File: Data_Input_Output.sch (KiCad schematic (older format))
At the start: 38 parts, among them K1 G5LE_1A4_DC3, K2 G5LE_1A4_DC3, P10 CONN_01X02, P11 CONN_01X02, P12 CONN_01X02, P3 CONN_01X04, P4 CONN_01X04, P5 CONN_01X04, P6 CONN_01X04, P7 CONN_01X02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

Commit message: completed first revision of the board.
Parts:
- P10, P11, P12, P7, P8, P9: footprint Connectors_JST:JST_PH_B2B-PH-K_02x2.00mm_Straight -> SPEX_Parts:ultraFitCONN_2
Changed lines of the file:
@@
 $EndDescr
 $Comp
-L GND #PWR062
+L GND #PWR063
 U 1 1 56EB177F
 P 5450 2550
-F 0 "#PWR062" H 5450 2300 50  0001 C CNN
+F 0 "#PWR063" H 5450 2300 50  0001 C CNN
 F 1 "GND" H 5450 2400 50  0000 C CNN
 F 2 "" H 5450 2550 60  0000 C CNN
@@
 Data_GND
 $Comp
-L +3.3V #PWR063
+L +3.3V #PWR064
 U 1 1 56EB1E10
 P 2500 950
-F 0 "#PWR063" H 2500 800 50  0001 C CNN
+F 0 "#PWR064" H 2500 800 50  0001 C CNN
 F 1 "+3.3V" H 2500 1090 50  0000 C CNN
 F 2 "" H 2500 950 60  0000 C CNN
@@
 $EndComp
 $Comp
-L GND #PWR064
+L GND #PWR065
 U 1 1 56EB1E33
 P 2500 1200
-F 0 "#PWR064" H 2500 950 50  0001 C CNN
+F 0 "#PWR065" H 2500 950 50  0001 C CNN
 F 1 "GND" H 2500 1050 50  0000 C CNN
 F 2 "" H 2500 1200 60  0000 C CNN
@@
 $EndComp
 $Comp
-L +3.3V #PWR065
+L +3.3V #PWR066
 U 1 1 56EB2146
 P 2550 2650
-F 0 "#PWR065" H 2550 2500 50  0001 C CNN
+F 0 "#PWR066" H 2550 2500 50  0001 C CNN
 F 1 "+3.3V" H 2550 2790 50  0000 C CNN
 F 2 "" H 2550 2650 60  0000 C CNN
@@
 $EndComp
 $Comp
-L GND #PWR066
+L GND #PWR067
 U 1 1 56EB216C
 P 2550 3950
-F 0 "#PWR066" H 2550 3700 50  0001 C CNN
+F 0 "#PWR067" H 2550 3700 50  0001 C CNN
 F 1 "GND" H 2550 3800 50  0000 C CNN
 F 2 "" H 2550 3950 60  0000 C CNN
@@
 $EndComp
 $Comp
-L GND #PWR067
+L GND #PWR068
 U 1 1 56EBFD84
 P 1900 5500
-F 0 "#PWR067" H 1900 5250 50  0001 C CNN
+F 0 "#PWR068" H 1900 5250 50  0001 C CNN
 F 1 "GND" H 1900 5350 50  0000 C CNN
 F 2 "" H 1900 5500 60  0000 C CNN
@@
 $EndComp
 $Comp
-L +3.3V #PWR068
+L +3.3V #PWR069
 U 1 1 56EBFDB9
 P 1900 4100
-F 0 "#PWR068" H 1900 3950 50  0001 C CNN
+F 0 "#PWR069" H 1900 3950 50  0001 C CNN
 F 1 "+3.3V" H 1900 4240 50  0000 C CNN
 F 2 "" H 1900 4100 60  0000 C CNN
@@
 SD_MISO
 $Comp
-L +3.3V #PWR069
+L +3.3V #PWR070
 U 1 1 56F427AD
 P 5400 1000
-F 0 "#PWR069" H 5400 850 50  0001 C CNN
+F 0 "#PWR070" H 5400 850 50  0001 C CNN
 F 1 "+3.3V" H 5400 1140 50  0000 C CNN
 F 2 "" H 5400 1000 60  0000 C CNN
@@
 $EndComp
 $Comp
-L +3.3V #PWR070
+L +3.3V #PWR071
 U 1 1 56F4344F
 P 6200 1600
-F 0 "#PWR070" H 6200 1450 50  0001 C CNN
+F 0 "#PWR071" H 6200 1450 50  0001 C CNN
 F 1 "+3.3V" H 6200 1740 50  0000 C CNN
 F 2 "" H 6200 1600 60  0000 C CNN
@@
 $EndComp
 $Comp
-L GND #PWR071
+L GND #PWR072
 U 1 1 56F43490
 P 6200 2400
-F 0 "#PWR071" H 6200 2150 50  0001 C CNN
+F 0 "#PWR072" H 6200 2150 50  0001 C CNN
 F 1 "GND" H 6200 2250 50  0000 C CNN
 F 2 "" H 6200 2400 60  0000 C CNN
@@
 SD_PWRCTRL
 $Comp
-L GND #PWR072
+L GND #PWR073
 U 1 1 56F6549F
 P 5950 3700
-F 0 "#PWR072" H 5950 3450 50  0001 C CNN
+F 0 "#PWR073" H 5950 3450 50  0001 C CNN
 F 1 "GND" H 5950 3550 50  0000 C CNN
 F 2 "" H 5950 3700 60  0000 C CNN
@@
 $EndComp
 $Comp
-L GND #PWR073
+L GND #PWR074
 U 1 1 56F66682
 P 5950 4650
-F 0 "#PWR073" H 5950 4400 50  0001 C CNN
+F 0 "#PWR074" H 5950 4400 50  0001 C CNN
 F 1 "GND" H 5950 4500 50  0000 C CNN
 F 2 "" H 5950 4650 60  0000 C CNN
@@
 $EndComp
 $Comp
-L GND #PWR074
+L GND #PWR075
 U 1 1 56F669B0
 P 5950 5600
-F 0 "#PWR074" H 5950 5350 50  0001 C CNN
+F 0 "#PWR075" H 5950 5350 50  0001 C CNN
 F 1 "GND" H 5950 5450 50  0000 C CNN
 F 2 "" H 5950 5600 60  0000 C CNN
@@
 Relay_2
 $Comp
-L +3.3V #PWR075
+L +3.3V #PWR076
 U 1 1 56F72165
 P 2850 6400
-F 0 "#PWR075" H 2850 6250 50  0001 C CNN
+F 0 "#PWR076" H 2850 6250 50  0001 C CNN
 F 1 "+3.3V" H 2850 6540 50  0000 C CNN
 F 2 "" H 2850 6400 60  0000 C CNN
@@
 $EndComp
 $Comp
-L +3.3V #PWR076
+L +3.3V #PWR077
 U 1 1 56F721B8
 P 5950 6400
-F 0 "#PWR076" H 5950 6250 50  0001 C CNN
+F 0 "#PWR077" H 5950 6250 50  0001 C CNN
 F 1 "+3.3V" H 5950 6540 50  0000 C CNN
 F 2 "" H 5950 6400 60  0000 C CNN
@@
 $EndComp
 $Comp
-L GND #PWR077
+L GND #PWR078
 U 1 1 56F72343
 P 1850 7600
-F 0 "#PWR077" H 1850 7350 50  0001 C CNN
+F 0 "#PWR078" H 1850 7350 50  0001 C CNN
 F 1 "GND" H 1850 7450 50  0000 C CNN
 F 2 "" H 1850 7600 60  0000 C CNN
@@
 $EndComp
 $Comp
-L GND #PWR078
+L GND #PWR079
 U 1 1 56F72396
 P 4950 7600
-F 0 "#PWR078" H 4950 7350 50  0001 C CNN
+F 0 "#PWR079" H 4950 7350 50  0001 C CNN
 F 1 "GND" H 4950 7450 50  0000 C CNN
 F 2 "" H 4950 7600 60  0000 C CNN
@@
 F 0 "P7" H 10350 3600 50  0000 C CNN
 F 1 "CONN_01X02" V 10450 3450 50  0000 C CNN
-F 2 "Connectors_JST:JST_PH_B2B-PH-K_02x2.00mm_Straight" H 10350 3450 50  0001 C CNN
+F 2 "SPEX_Parts:ultraFitCONN_2" H 10350 3450 50  0001 C CNN
 F 3 "" H 10350 3450 50  0000 C CNN
 	1    10350 3450
@@
 F 0 "P8" H 10350 4100 50  0000 C CNN
 F 1 "CONN_01X02" V 10450 3950 50  0000 C CNN
-F 2 "Connectors_JST:JST_PH_B2B-PH-K_02x2.00mm_Straight" H 10350 3950 50  0001 C CNN
+F 2 "SPEX_Parts:ultraFitCONN_2" H 10350 3950 50  0001 C CNN
 F 3 "" H 10350 3950 50  0000 C CNN
 	1    10350 3950
@@
 F 0 "P9" H 10350 4600 50  0000 C CNN
 F 1 "CONN_01X02" V 10450 4450 50  0000 C CNN
-F 2 "Connectors_JST:JST_PH_B2B-PH-K_02x2.00mm_Straight" H 10350 4450 50  0001 C CNN
+F 2 "SPEX_Parts:ultraFitCONN_2" H 10350 4450 50  0001 C CNN
 F 3 "" H 10350 4450 50  0000 C CNN
 	1    10350 4450
@@
 F 0 "P10" H 10350 5100 50  0000 C CNN
 F 1 "CONN_01X02" V 10450 4950 50  0000 C CNN
-F 2 "Connectors_JST:JST_PH_B2B-PH-K_02x2.00mm_Straight" H 10350 4950 50  0001 C CNN
+F 2 "SPEX_Parts:ultraFitCONN_2" H 10350 4950 50  0001 C CNN
 F 3 "" H 10350 4950 50  0000 C CNN
 	1    10350 4950
@@
 F 0 "P11" H 10350 5600 50  0000 C CNN
 F 1 "CONN_01X02" V 10450 5450 50  0000 C CNN
-F 2 "Connectors_JST:JST_PH_B2B-PH-K_02x2.00mm_Straight" H 10350 5450 50  0001 C CNN
+F 2 "SPEX_Parts:ultraFitCONN_2" H 10350 5450 50  0001 C CNN
 F 3 "" H 10350 5450 50  0000 C CNN
 	1    10350 5450
@@
 F 0 "P12" H 10350 6150 50  0000 C CNN
 F 1 "CONN_01X02" V 10450 6000 50  0000 C CNN
-F 2 "Connectors_JST:JST_PH_B2B-PH-K_02x2.00mm_Straight" H 10350 6000 50  0001 C CNN
+F 2 "SPEX_Parts:ultraFitCONN_2" H 10350 6000 50  0001 C CNN
 F 3 "" H 10350 6000 50  0000 C CNN
 	1    10350 6000
@@
 	10050 6050 10150 6050
 $Comp
-L GND #PWR079
+L GND #PWR080
 U 1 1 57038625
 P 9450 2600
-F 0 "#PWR079" H 9450 2350 50  0001 C CNN
+F 0 "#PWR080" H 9450 2350 50  0001 C CNN
 F 1 "GND" H 9450 2450 50  0000 C CNN
 F 2 "" H 9450 2600 60  0000 C CNN
@@
 $EndComp
 $Comp
-L GND #PWR080
+L GND #PWR081
 U 1 1 5703869C
 P 9450 1700
-F 0 "#PWR080" H 9450 1450 50  0001 C CNN
+F 0 "#PWR081" H 9450 1450 50  0001 C CNN
 F 1 "GND" H 9450 1550 50  0000 C CNN
 F 2 "" H 9450 1700 60  0000 C CNN
@@
 	9450 2500 9450 2600
 $Comp
-L +3.3V #PWR081
+L +3.3V #PWR082
 U 1 1 57038AFB
 P 9450 1200
-F 0 "#PWR081" H 9450 1050 50  0001 C CNN
+F 0 "#PWR082" H 9450 1050 50  0001 C CNN
 F 1 "+3.3V" H 9450 1340 50  0000 C CNN
 F 2 "" H 9450 1200 60  0000 C CNN
@@
 $EndComp
 $Comp
-L +3.3V #PWR082
+L +3.3V #PWR083
 U 1 1 57038B72
 P 9450 2100
-F 0 "#PWR082" H 9450 1950 50  0001 C CNN
+F 0 "#PWR083" H 9450 1950 50  0001 C CNN
 F 1 "+3.3V" H 9450 2240 50  0000 C CNN
 F 2 "" H 9450 2100 60  0000 C CNN
@@
 $EndComp
 $Comp
-L +3.3V #PWR083
+L +3.3V #PWR084
 U 1 1 57039D7A
 P 8300 1200
-F 0 "#PWR083" H 8300 1050 50  0001 C CNN
+F 0 "#PWR084" H 8300 1050 50  0001 C CNN
 F 1 "+3.3V" H 8300 1340 50  0000 C CNN
 F 2 "" H 8300 1200 60  0000 C CNN
@@
 $EndComp
 $Comp
-L GND #PWR084
+L GND #PWR085
 U 1 1 57039E1D
 P 8300 1700
-F 0 "#PWR084" H 8300 1450 50  0001 C CNN
+F 0 "#PWR085" H 8300 1450 50  0001 C CNN
 F 1 "GND" H 8300 1550 50  0000 C CNN
 F 2 "" H 8300 1700 60  0000 C CNN
@@
 $EndComp
 $Comp
-L +3.3V #PWR085
+L +3.3V #PWR086
 U 1 1 57033FCB
 P 8300 2100
-F 0 "#PWR085" H 8300 1950 50  0001 C CNN
+F 0 "#PWR086" H 8300 1950 50  0001 C CNN
 F 1 "+3.3V" H 8300 2240 50  0000 C CNN
 F 2 "" H 8300 2100 60  0000 C CNN
@@
 $EndComp
 $Comp
-L GND #PWR086
+L GND #PWR087
 U 1 1 57033FD1
 P 8300 2600
-F 0 "#PWR086" H 8300 2350 50  0001 C CNN
+F 0 "#PWR087" H 8300 2350 50  0001 C CNN
 F 1 "GND" H 8300 2450 50  0000 C CNN
 F 2 "" H 8300 2600 60  0000 C CNN
@@
 UART_RX_out
 $Comp
-L +3.3V #PWR087
+L +3.3V #PWR088
 U 1 1 570406FF
 P 10000 3300
-F 0 "#PWR087" H 10000 3150 50  0001 C CNN
+F 0 "#PWR088" H 10000 3150 50  0001 C CNN
 F 1 "+3.3V" H 10000 3440 50  0000 C CNN
 F 2 "" H 10000 3300 60  0000 C CNN
@@
 	10000 3300 10000 3500
 $Comp
-L +5V #PWR088
+L +5V #PWR089
 U 1 1 57040BC0
 P 10000 3800
-F 0 "#PWR088" H 10000 3650 50  0001 C CNN
+F 0 "#PWR089" H 10000 3650 50  0001 C CNN
 F 1 "+5V" H 10000 3940 50  0000 C CNN
 F 2 "" H 10000 3800 50  0000 C CNN
@@
 5V_in
 $Comp
-L +5V #PWR089
+L +5V #PWR090
 U 1 1 57044D2C
 P 2750 950
-F 0 "#PWR089" H 2750 800 50  0001 C CNN
+F 0 "#PWR090" H 2750 800 50  0001 C CNN
 F 1 "+5V" H 2750 1090 50  0000 C CNN
 F 2 "" H 2750 950 50  0000 C CNN
@@
 	2750 1000 2950 1000
 $Comp
-L GND #PWR090
+L GND #PWR091
 U 1 1 57047398
 P 10050 6150
-F 0 "#PWR090" H 10050 5900 50  0001 C CNN
+F 0 "#PWR091" H 10050 5900 50  0001 C CNN
 F 1 "GND" H 10050 6000 50  0000 C CNN
 F 2 "" H 10050 6150 60  0000 C CNN

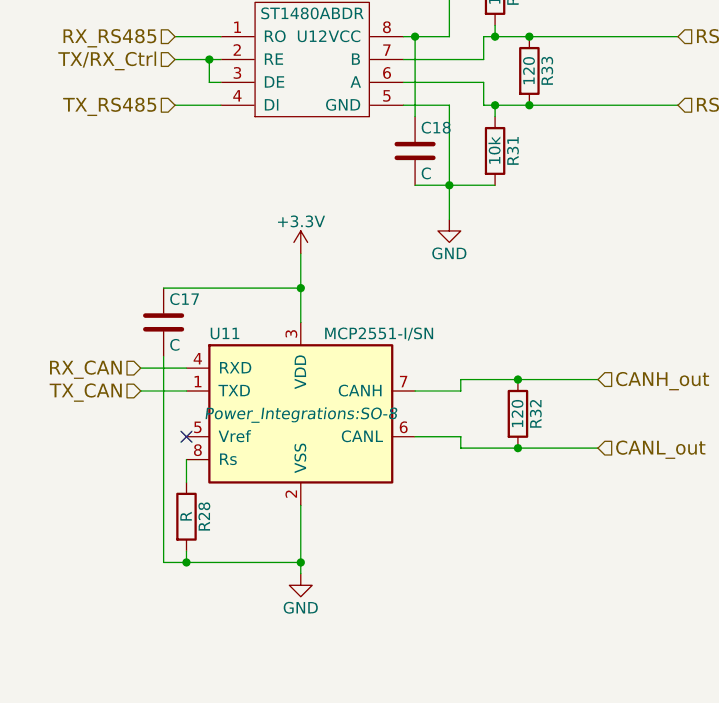
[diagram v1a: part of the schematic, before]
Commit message: updated passive values
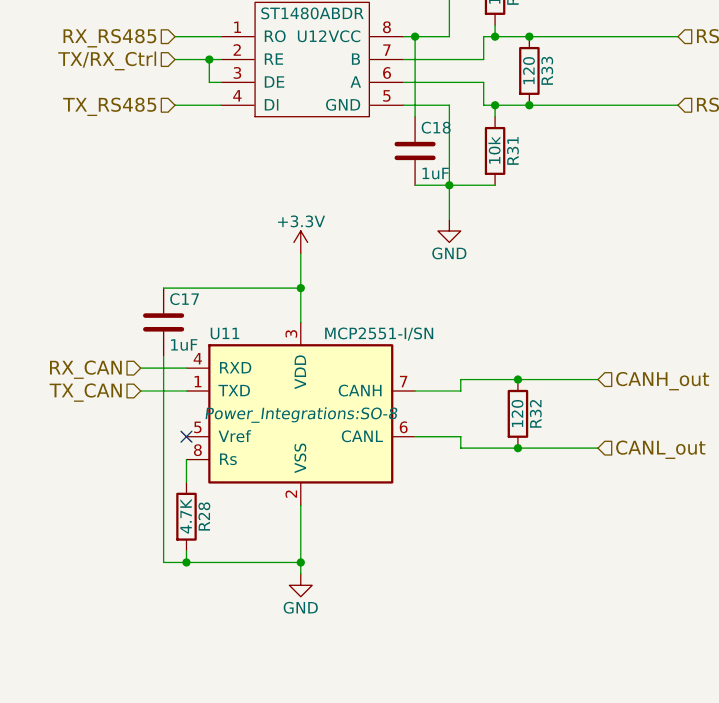
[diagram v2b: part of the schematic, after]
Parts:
- C17, C18: value C -> 1uF
- R28: value R -> 4.7K
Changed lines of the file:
@@
 P 2400 3650
 F 0 "C18" H 2425 3750 50  0000 L CNN
-F 1 "C" H 2425 3550 50  0000 L CNN
+F 1 "1uF" H 2425 3550 50  0000 L CNN
 F 2 "Capacitors_SMD:C_0603" H 2438 3500 50  0001 C CNN
 F 3 "" H 2400 3650 50  0000 C CNN
@@
 P 1400 5250
 F 0 "R28" V 1480 5250 50  0000 C CNN
-F 1 "R" V 1400 5250 50  0000 C CNN
+F 1 "4.7K" V 1400 5250 50  0000 C CNN
 F 2 "Resistors_SMD:R_0603" V 1330 5250 50  0001 C CNN
 F 3 "" H 1400 5250 50  0000 C CNN
@@
 P 1300 4400
 F 0 "C17" H 1325 4500 50  0000 L CNN
-F 1 "C" H 1325 4300 50  0000 L CNN
+F 1 "1uF" H 1325 4300 50  0000 L CNN
 F 2 "Capacitors_SMD:C_0603" H 1338 4250 50  0001 C CNN
 F 3 "" H 1300 4400 50  0000 C CNN

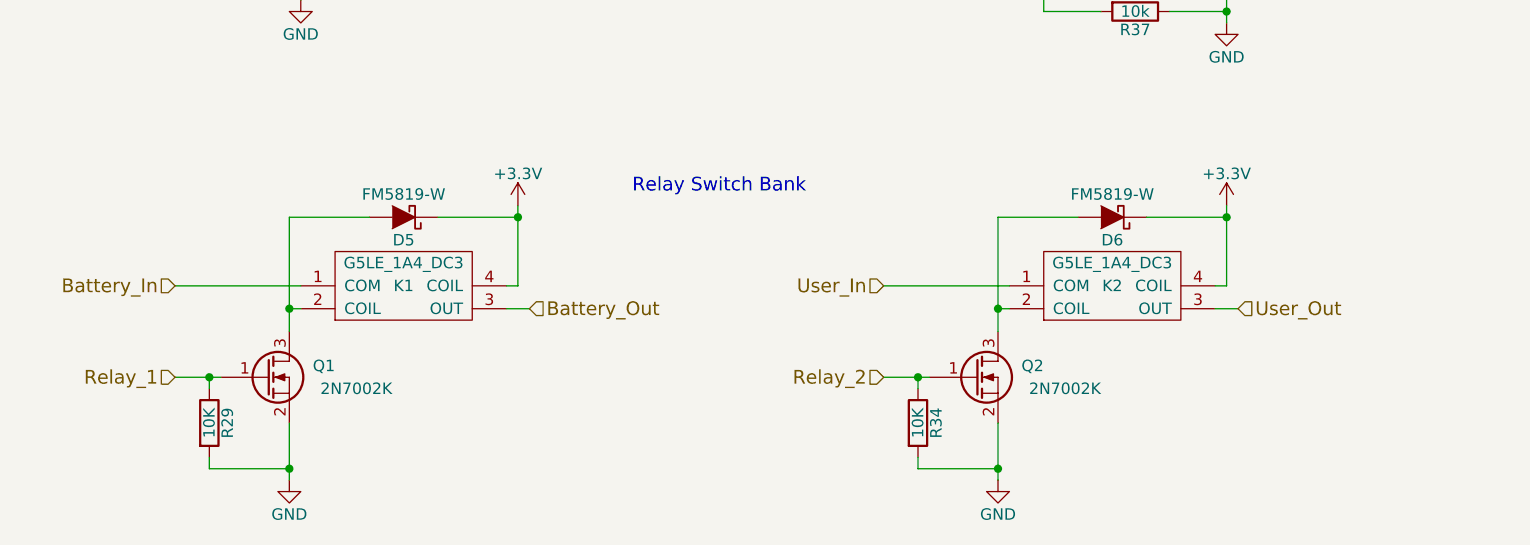
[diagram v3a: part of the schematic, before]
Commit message: rev 2 of hab board in progress
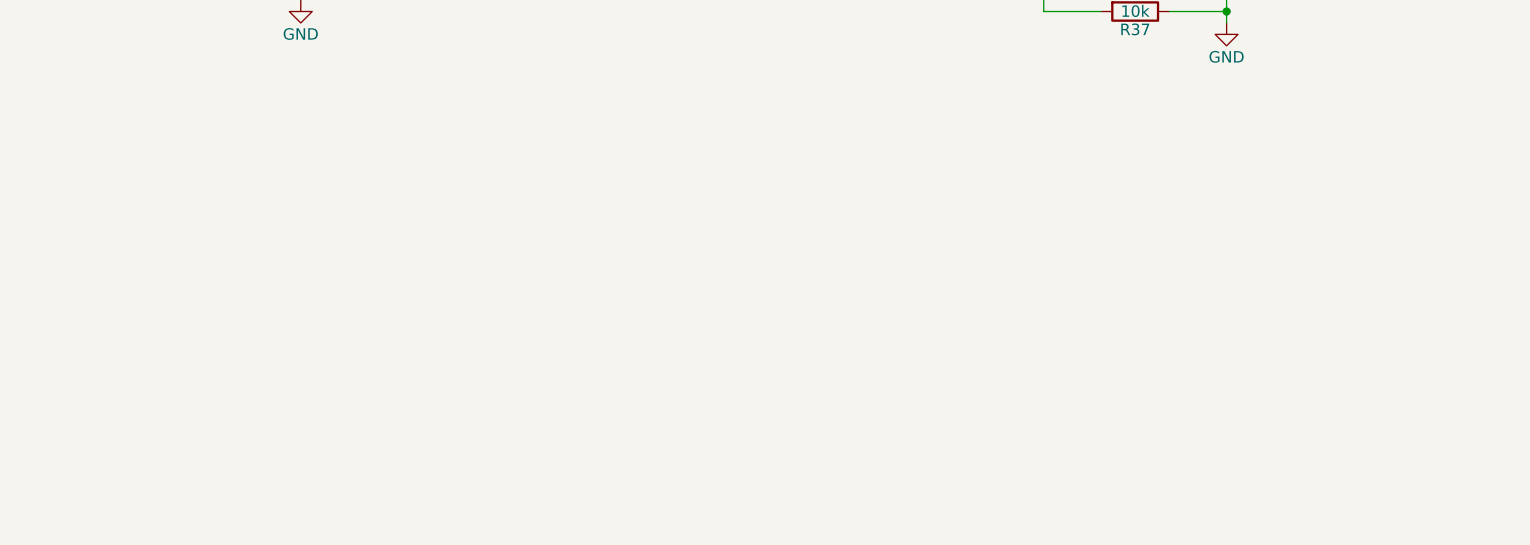
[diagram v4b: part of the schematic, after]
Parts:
- removed D5, D6: FM5819-W, Diodes_SMD:SMA_Standard, symbol FM5819-W
- removed K1, K2: G5LE_1A4_DC3, SPEX_Parts:G5LE-1A4-DC3, symbol G5LE_1A4_DC3
- removed Q1, Q2: 2N7002K, TO_SOT_Packages_SMD:SOT-23, symbol 2N7002K
- removed R29, R34: 10K, Resistors_SMD:R_0603, symbol R
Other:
- note removed: "Relay Switch Bank\n"

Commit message: updates per week 1 meeting
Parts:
- removed C17: 1uF, Capacitors_SMD:C_0603, symbol C
- removed R28: 4.7K, Resistors_SMD:R_0603, symbol R
- removed R32: 120, Resistors_SMD:R_0603, symbol R
- removed U11: MCP2551-I/SN, Power_Integrations:SO-8, symbol MCP2551-I/SN
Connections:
- net CANH_out renamed I/O1
- net CANL_out renamed I/O2
- no-connect marks 3 -> 2
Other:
- moved on the sheet: C19, C20, P3, P4, P5, P6, Q3, R38, U13
